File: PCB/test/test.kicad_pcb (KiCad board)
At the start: 2 copper layers, 40.2 x 30 mm, 58 parts, among them CN5 UFL, SW2 MLL1200S_TE, U1 STM32WBxx_QFN48, U2 USBLC6-2SC6, U3 LD3985M33R, X1 NX2016_32MHz, X2 NX2012_32K768Hz

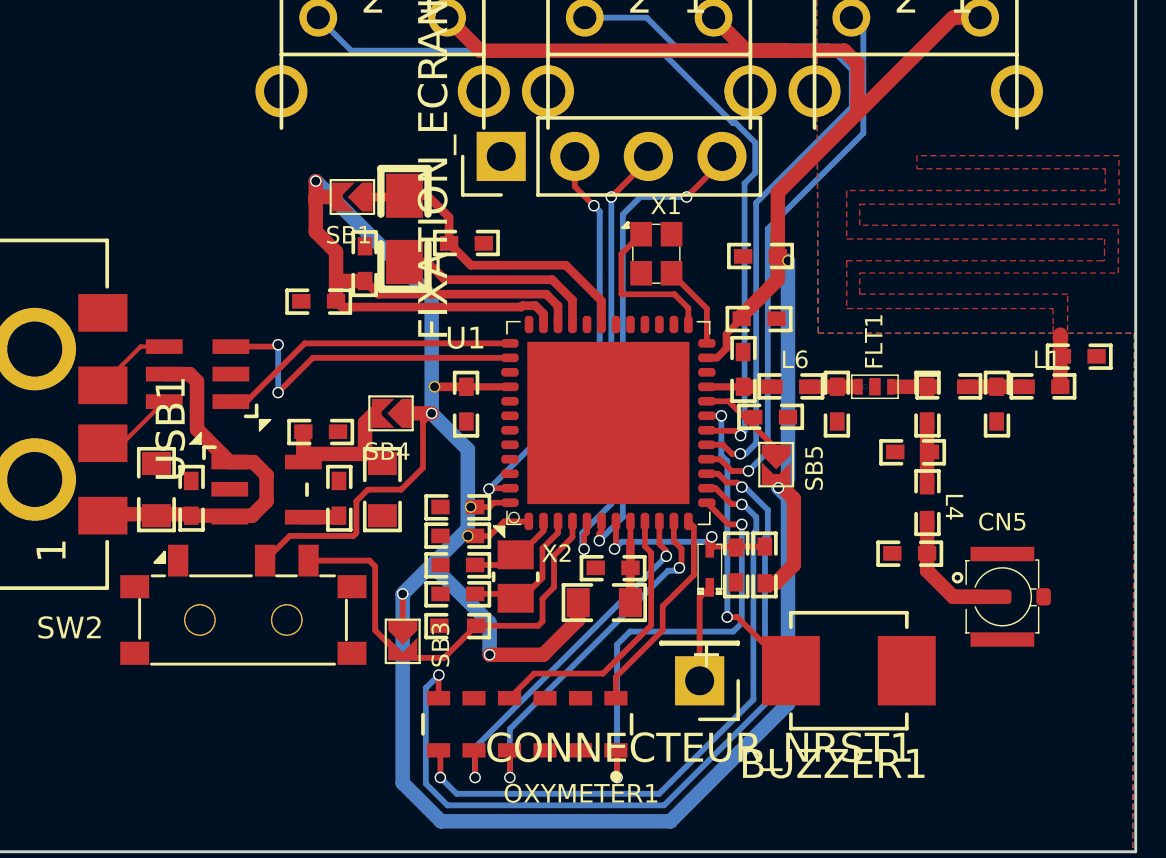
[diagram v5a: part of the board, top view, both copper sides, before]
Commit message: ajout des grounds
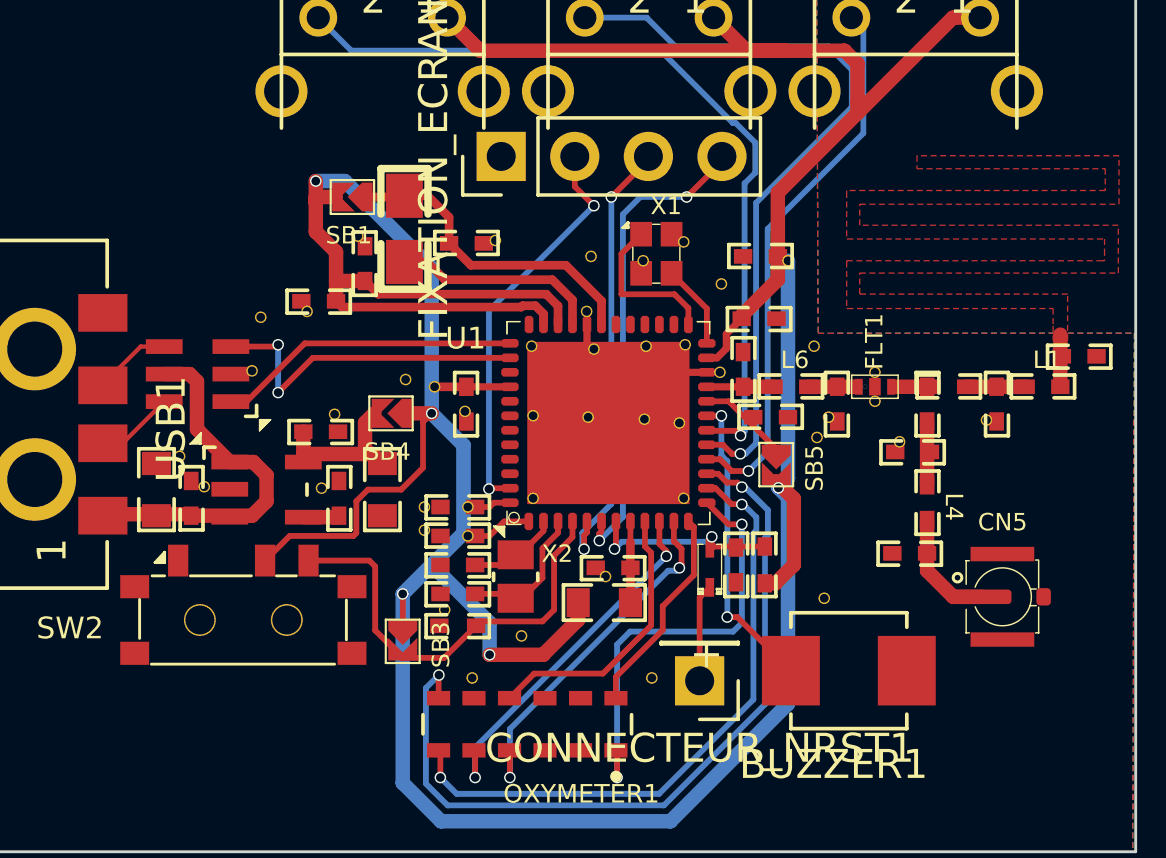
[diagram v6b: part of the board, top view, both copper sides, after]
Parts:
- added ?: , , F.Cu at (137.7, 90.4)
- added ?: , , F.Cu at (144.2, 91.3)
- added ?: , , F.Cu at (136.2, 93.0)
- added ?: , , F.Cu at (142.4, 99.2)
- added ?: , , F.Cu at (129.3, 99.5)
- added ?: , , F.Cu at (142.1, 90.5)
- added ?: , , F.Cu at (132.3, 90.5)
- added ?: , , F.Cu at (132.4, 92.8)
- added ?: , , F.Cu at (136.5, 101.9)
- added ?: , , F.Cu at (125.5, 92.8)
- added ?: , , F.Cu at (120.2, 94.2)
- added ?: , , F.Cu at (130.3, 101.9)
- added ?: , , F.Cu at (134.2, 89.2)
- added ?: , , F.Cu at (138.9, 88.3)
- added ?: , , F.Cu at (125.1, 95.3)
- added ?: , , F.Cu at (123.0, 89.5)
- added ?: , , F.Cu at (128.7, 96.8)
- added ?: , , F.Cu at (144.2, 92.3)
- added ?: , , F.Cu at (130.1, 92.7)
- added ?: , , F.Cu at (145.1, 93.8)
- added ?: , , F.Cu at (137.6, 95.7)
- added ?: , , F.Cu at (134.5, 90.5)
- added ?: , , F.Cu at (142.2, 93.6)
- added ?: , , F.Cu at (136.3, 90.5)
- added ?: , , F.Cu at (136.2, 87.5)
- added ?: , , F.Cu at (134.3, 92.9)
- added ?: , , F.Cu at (132.0, 100.5)
- added ?: , , F.Cu at (128.7, 96.0)
- added ?: , , F.Cu at (128.0, 91.6)
- added ?: , , F.Cu at (132.4, 95.7)
- added ?: , , F.Cu at (138.8, 91.3)
- added ?: , , F.Cu at (137.6, 86.8)
- added ?: , , F.Cu at (137.4, 93.1)
- added ?: , , F.Cu at (134.9, 98.4)
- added ?: , , F.Cu at (131.1, 86.8)
- added ?: , , F.Cu at (148.1, 93.0)
- added ?: , , F.Cu at (126.3, 86.7)
- added ?: , , F.Cu at (121.0, 95.3)
- added ?: , , F.Cu at (124.6, 89.2)
- added ?: , , F.Cu at (122.7, 91.3)
- added ?: , , F.Cu at (134.4, 87.3)
- added ?: , , F.Cu at (142.6, 92.9)
- moved ? 0.10 mm to (130.2, 96.0)
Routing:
- net GND: track 0.00 -> 7.83 mm

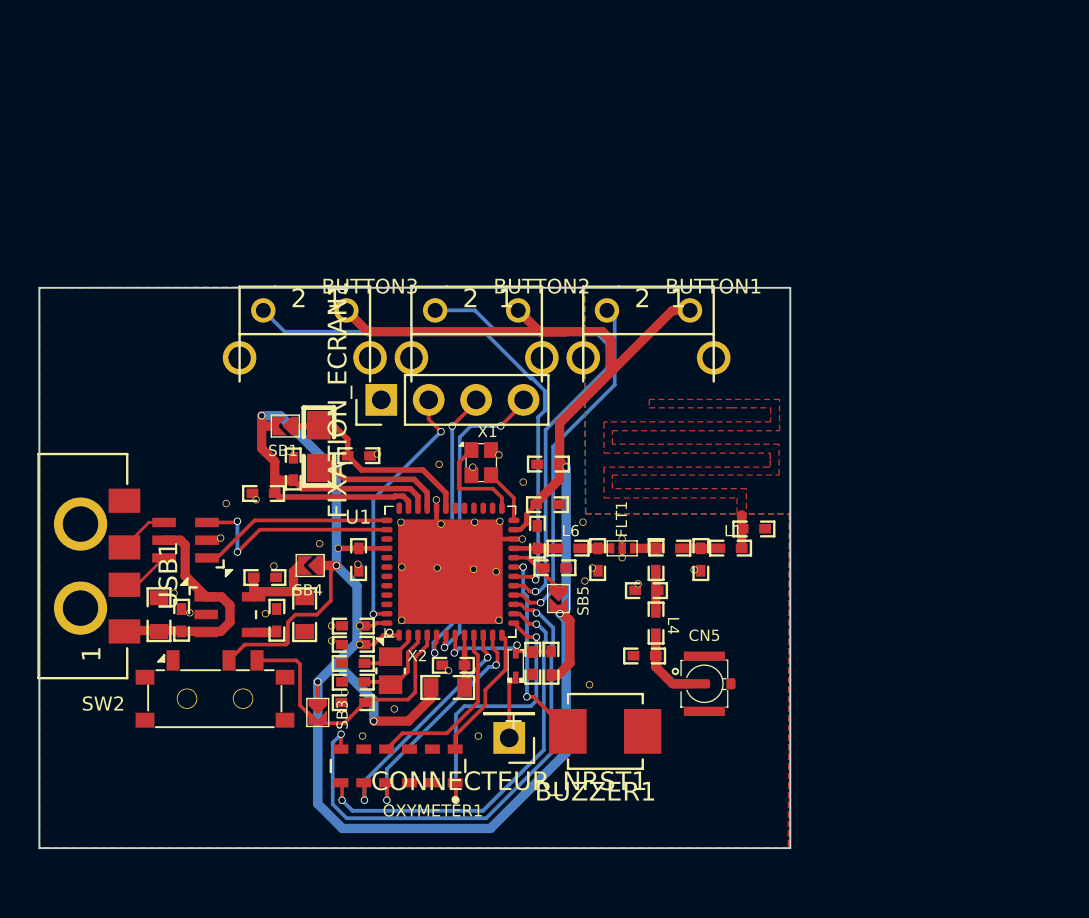
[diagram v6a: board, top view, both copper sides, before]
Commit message: fix through hole gnd
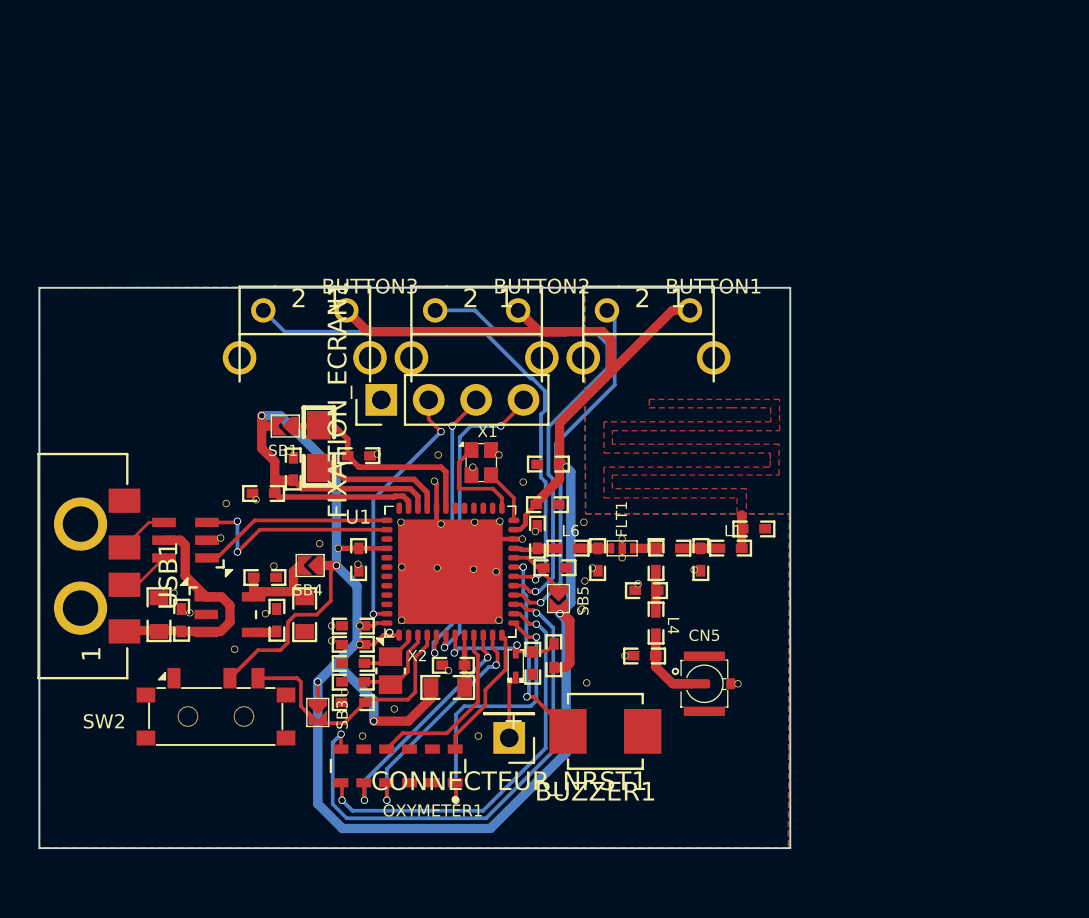
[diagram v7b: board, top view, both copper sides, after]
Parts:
- added ?: , , F.Cu at (144.3, 97.6)
- added ?: , , F.Cu at (142.1, 95.1)
- added ?: , , F.Cu at (139.6, 91.0)
- added ?: , , F.Cu at (150.4, 99.1)
- added ?: , , F.Cu at (123.5, 97.2)
- moved ? 1.00 mm to (134.2, 88.2)
- moved SW2 0.95 mm to (122.5, 100.9)
- moved ? 0.50 mm to (134.3, 86.8)
- moved R1 0.43 mm to (140.6, 97.6)
- moved ? 0.18 mm to (142.3, 99.0)
- moved ? 0.05 mm to (142.2, 90.5)
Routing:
- net GND: track 7.83 -> 9.33 mm
- net BOOT0: track 15.2 -> 14.2 mm
- net Net-(C10-Pad1): track 11.0 -> 11.7 mm

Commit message: small error fixes
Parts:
- added ?: , , F.Cu at (133.2, 100.4)
- moved ? 0.15 mm to (132.0, 100.6)
- moved ? 0.11 mm to (142.1, 95.2)
- moved SB5 0.06 mm to (140.9, 94.6)
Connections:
- BUTTON1 pad GND1: GND -> (no net)
- BUTTON3 pad GND2: unconnected-(BUTTON3-PadGND2) -> GND
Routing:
- net 3V3: track 143.3 -> 141.7 mm
